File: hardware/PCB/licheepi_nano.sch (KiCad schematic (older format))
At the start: 4 parts

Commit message: update for schematic,
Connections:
- net PE10: now reaches U?.49 (PE10/CSI_D7/SPI1_SO)
- net PE9: now reaches U?.51 (PE9/CSI_D6/SPI1_CLK)
- net PE5: now reaches U?.59 (PE5/DA_IN/CSI_D2)
- net PE4: now reaches U?.61 (PE4/DA_LRCK/CSI_D1)
- net PE3: now reaches U?.63 (PE3/DA_BCLK/CSI_D0)
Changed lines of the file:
@@
 Wire Wire Line
 	10850 950  10850 1050
-Text Label 8900 3250 2    50   ~ 0
+Text Label 8700 3250 2    50   ~ 0
 FEL_ENABLE
 Wire Wire Line
-	8900 3250 8050 3250
+	8700 3250 8050 3250
 $Comp
 L customized_power:+5V #PWR?
@@
 Wire Wire Line
 	3850 4350 2850 4350
-Text Label 9050 3550 2    50   ~ 0
+Text Label 8700 3550 2    50   ~ 0
 UART1_TX
 Wire Wire Line
-	8050 3550 9050 3550
-Text Label 9050 3750 2    50   ~ 0
+	8050 3550 8700 3550
+Text Label 8700 3750 2    50   ~ 0
 UART1_RX
 Wire Wire Line
-	8050 3750 9050 3750
+	8050 3750 8700 3750
+Text Label 8700 4150 2    50   ~ 0
+PE10
+Wire Wire Line
+	8050 4150 8700 4150
+Text Label 8700 3950 2    50   ~ 0
+PE9
+Wire Wire Line
+	8050 3950 8700 3950
+Text Label 8700 3150 2    50   ~ 0
+PE5
+Wire Wire Line
+	8050 3150 8700 3150
+Text Label 8700 2950 2    50   ~ 0
+PE4
+Wire Wire Line
+	8050 2950 8700 2950
+Text Label 8700 2750 2    50   ~ 0
+PE3
+Wire Wire Line
+	8050 2750 8700 2750
 $EndSCHEMATC

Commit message: update requirements,
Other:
- note added: "REQUIREMENTS:\nADD I2C CONN TO SHT22"
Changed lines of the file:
@@
 Wire Wire Line
 	8050 2750 8700 2750
+Text Notes 700  900  0    50   ~ 0
+REQUIREMENTS:\nADD I2C CONN TO SHT22
 $EndSCHEMATC

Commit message: update pcb,
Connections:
- net UART1_RX: no longer U?.53 (PE8/CSI_D5/SPI_SI/UART2_RX)
- net UART1_TX: no longer U?.55 (PE7/SPI1_CS/CSI_D4/UART2_TX)
- net PE2: now reaches U?.2 (PE2/CSI_PCLK)
- net SDC1_D1: now reaches U?.46 (SDC0-D1)
- net SDC1_D0: now reaches U?.48 (SDC0-D0)
- net SDC1_CLK: now reaches U?.50 (SDC0-CLK)
- net SDC1_CMD: now reaches U?.52 (SDC0-CMD)
- net SDC1_D3: now reaches U?.54 (SDC0-D3)
- net SDC1_D2: now reaches U?.56 (SDC0-D2)
- new net UART2_RX: U?.53 (PE8/CSI_D5/SPI_SI/UART2_RX)
- new net UART2_TX: U?.55 (PE7/SPI1_CS/CSI_D4/UART2_TX)
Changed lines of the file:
@@
 $Descr A4 11693 8268
 encoding utf-8
-Sheet 2 4
+Sheet 2 5
 Title ""
 Date ""
@@
 P 10850 850
 AR Path="/5E87CEF1/5E88E558" Ref="#PWR?"  Part="1"
-AR Path="/5E87A116/5E88E558" Ref="#PWR?"  Part="1"
-F 0 "#PWR?" H 10850 700 50  0001 C CNN
+AR Path="/5E87A116/5E88E558" Ref="#PWR0103"  Part="1"
+F 0 "#PWR0103" H 10850 700 50  0001 C CNN
 F 1 "+5V" H 10865 1023 50  0000 C CNN
 F 2 "" H 10850 850 50  0001 C CNN
@@
 $EndComp
 $Comp
-L power:GND #PWR?
+L power:GND #PWR0104
 U 1 1 5E88E55E
 P 10850 1900
-F 0 "#PWR?" H 10850 1650 50  0001 C CNN
+F 0 "#PWR0104" H 10850 1650 50  0001 C CNN
 F 1 "GND" H 10855 1727 50  0000 C CNN
 F 2 "" H 10850 1900 50  0001 C CNN
@@
 Wire Wire Line
 	10850 950  10850 1050
-Text Label 8700 3250 2    50   ~ 0
+Text Label 9750 3250 2    50   ~ 0
 FEL_ENABLE
-Wire Wire Line
-	8700 3250 8050 3250
 $Comp
 L customized_power:+5V #PWR?
@@
 P 5550 1650
 AR Path="/5E87CEF1/5E895245" Ref="#PWR?"  Part="1"
-AR Path="/5E87A116/5E895245" Ref="#PWR?"  Part="1"
-F 0 "#PWR?" H 5550 1500 50  0001 C CNN
+AR Path="/5E87A116/5E895245" Ref="#PWR0105"  Part="1"
+F 0 "#PWR0105" H 5550 1500 50  0001 C CNN
 F 1 "+5V" V 5565 1778 50  0000 L CNN
 F 2 "" H 5550 1650 50  0001 C CNN
@@
 $EndComp
 $Comp
-L power:GND #PWR?
+L power:GND #PWR0106
 U 1 1 5E896ED8
 P 6300 1650
-F 0 "#PWR?" H 6300 1400 50  0001 C CNN
+F 0 "#PWR0106" H 6300 1400 50  0001 C CNN
 F 1 "GND" V 6305 1522 50  0000 R CNN
 F 2 "" H 6300 1650 50  0001 C CNN
@@
 P 2950 3350
 AR Path="/5E87CEF1/5E89C8DE" Ref="#PWR?"  Part="1"
-AR Path="/5E87A116/5E89C8DE" Ref="#PWR?"  Part="1"
-F 0 "#PWR?" H 2950 3200 50  0001 C CNN
+AR Path="/5E87A116/5E89C8DE" Ref="#PWR0107"  Part="1"
+F 0 "#PWR0107" H 2950 3200 50  0001 C CNN
 F 1 "+5V" V 2965 3478 50  0000 L CNN
 F 2 "" H 2950 3350 50  0001 C CNN
@@
 	2950 3350 3850 3350
 $Comp
-L power:GND #PWR?
+L power:GND #PWR0108
 U 1 1 5E89D911
 P 2950 3550
-F 0 "#PWR?" H 2950 3300 50  0001 C CNN
+F 0 "#PWR0108" H 2950 3300 50  0001 C CNN
 F 1 "GND" V 2955 3422 50  0000 R CNN
 F 2 "" H 2950 3550 50  0001 C CNN
@@
 	3850 4350 2850 4350
 Text Label 8700 3550 2    50   ~ 0
-UART1_TX
-Wire Wire Line
-	8050 3550 8700 3550
+UART2_TX
 Text Label 8700 3750 2    50   ~ 0
-UART1_RX
-Wire Wire Line
-	8050 3750 8700 3750
+UART2_RX
 Text Label 8700 4150 2    50   ~ 0
 PE10
@@
 Text Label 8700 3150 2    50   ~ 0
 PE5
-Wire Wire Line
-	8050 3150 8700 3150
 Text Label 8700 2950 2    50   ~ 0
 PE4
-Wire Wire Line
-	8050 2950 8700 2950
 Text Label 8700 2750 2    50   ~ 0
 PE3
-Wire Wire Line
-	8050 2750 8700 2750
 Text Notes 700  900  0    50   ~ 0
 REQUIREMENTS:\nADD I2C CONN TO SHT22
+Text HLabel 8850 3450 2    50   BiDi ~ 0
+SDC1_D2
+Text HLabel 8850 4450 2    50   BiDi ~ 0
+SDC1_D1
+Text HLabel 8850 4250 2    50   BiDi ~ 0
+SDC1_D0
+Text HLabel 8850 4050 2    50   BiDi ~ 0
+SDC1_CLK
+Text HLabel 8850 3850 2    50   BiDi ~ 0
+SDC1_CMD
+Text HLabel 8850 3650 2    50   BiDi ~ 0
+SDC1_D3
+Wire Wire Line
+	8050 3450 8850 3450
+Wire Wire Line
+	8050 3650 8850 3650
+Wire Wire Line
+	8050 3850 8850 3850
+Wire Wire Line
+	8050 4050 8850 4050
+Wire Wire Line
+	8850 4250 8050 4250
+Wire Wire Line
+	8850 4450 8050 4450
+Text HLabel 9900 3250 2    50   Input ~ 0
+FEL_ENABLE
+Wire Wire Line
+	8050 3250 9900 3250
+Text Label 9050 3250 2    50   ~ 0
+SPI0-CLK
+Text Label 2850 2750 0    50   ~ 0
+PE2
+Wire Wire Line
+	2800 2750 3850 2750
+Text HLabel 2800 2750 0    50   Input ~ 0
+PE2
+Text HLabel 8800 2750 2    50   Input ~ 0
+PE3
+Wire Wire Line
+	8050 2750 8800 2750
+Text HLabel 8800 2950 2    50   Input ~ 0
+PE4
+Text HLabel 8800 3150 2    50   Output ~ 0
+PE5
+Wire Wire Line
+	8050 2950 8800 2950
+Wire Wire Line
+	8050 3150 8800 3150
+Text HLabel 2850 2950 0    50   Input ~ 0
+UART0_TX
+Text HLabel 2850 3150 0    50   Input ~ 0
+UART0_RX
+Text HLabel 2850 4550 0    50   Input ~ 0
+UART1_TX
+Text HLabel 2850 4350 0    50   Input ~ 0
+UART1_RX
+Text HLabel 8850 3750 2    50   Input ~ 0
+UART2_RX
+Text HLabel 8850 3550 2    50   Input ~ 0
+UART2_TX
+Wire Wire Line
+	8050 3550 8850 3550
+Wire Wire Line
+	8050 3750 8850 3750
 $EndSCHEMATC

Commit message: update before change,
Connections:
- net SPI0_CS: now reaches U?.23 (LCD-D18)
- net SPI0_MOSI: now reaches U?.24 (LCD-D19)
- net SPI0_CLK: now reaches U?.25 (LCD-D20)
- net SPI0_MISO: now reaches U?.26 (LCD-D21)
- net I2C0-SDA: now reaches U?.45 (PE12/TWI0_SDA)
- net I2C0-SCK: now reaches U?.47 (PE11/TWI0_SCK)
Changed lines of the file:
@@
 $Descr A4 11693 8268
 encoding utf-8
-Sheet 2 5
+Sheet 5 6
 Title ""
 Date ""
@@
 Wire Wire Line
 	8050 3750 8850 3750
+Text HLabel 8850 4350 2    50   BiDi ~ 0
+I2C0-SCK
+Text HLabel 8850 4550 2    50   BiDi ~ 0
+I2C0-SDA
+Wire Wire Line
+	8050 4350 8850 4350
+Wire Wire Line
+	8850 4550 8050 4550
+Text HLabel 5000 6250 3    50   Input ~ 0
+SPI0_CS
+Text HLabel 5100 6250 3    50   Input ~ 0
+SPI0_MOSI
+Text HLabel 5200 6250 3    50   Input ~ 0
+SPI0_CLK
+Text HLabel 5300 6250 3    50   Input ~ 0
+SPI0_MISO
+Wire Wire Line
+	5000 5700 5000 6250
+Wire Wire Line
+	5100 5700 5100 6250
+Wire Wire Line
+	5200 5700 5200 6250
+Wire Wire Line
+	5300 5700 5300 6250
 $EndSCHEMATC

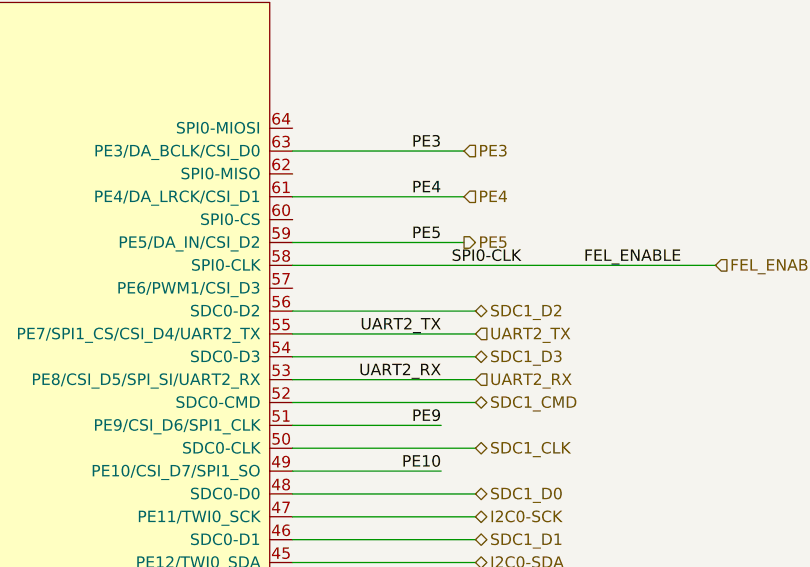
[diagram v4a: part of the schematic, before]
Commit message: pcb: update for selective buzzer input,
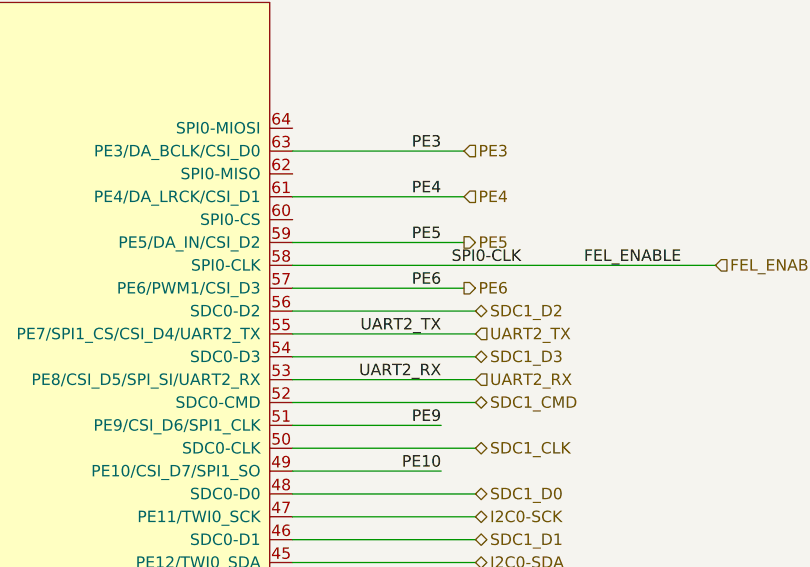
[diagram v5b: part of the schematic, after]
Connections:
- net PE6: now reaches U?.57 (PE6/PWM1/CSI_D3)
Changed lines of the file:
@@
 Wire Wire Line
 	5300 5700 5300 6250
+Text Label 8700 3350 2    50   ~ 0
+PE6
+Text HLabel 8800 3350 2    50   Output ~ 0
+PE6
+Wire Wire Line
+	8050 3350 8800 3350
 $EndSCHEMATC
